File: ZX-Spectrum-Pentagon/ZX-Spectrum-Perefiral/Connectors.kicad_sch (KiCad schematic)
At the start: 4 parts, among them J1 IDE, J2 FDD

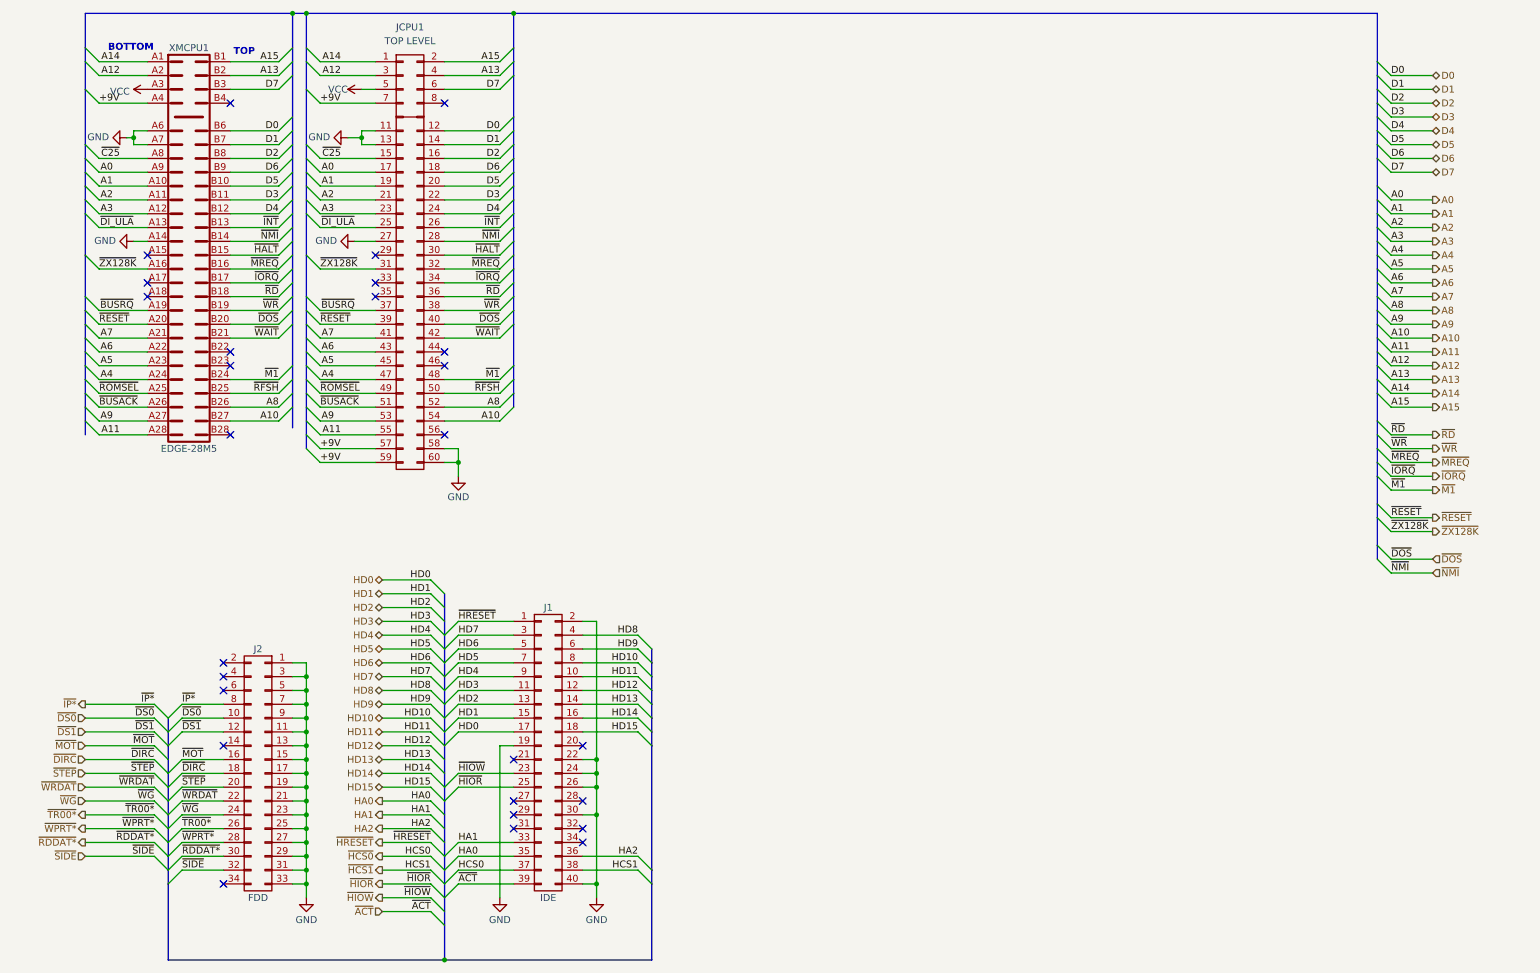
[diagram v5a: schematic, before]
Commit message: FDControlers rename from VCC1 to VDD zx_custom_symbol add connector Conn_02x32_Odd_Even ZX-Spectrum-Pentagon rename from +9V to POWER ZX-Spectrum-Perefiral improve schematic
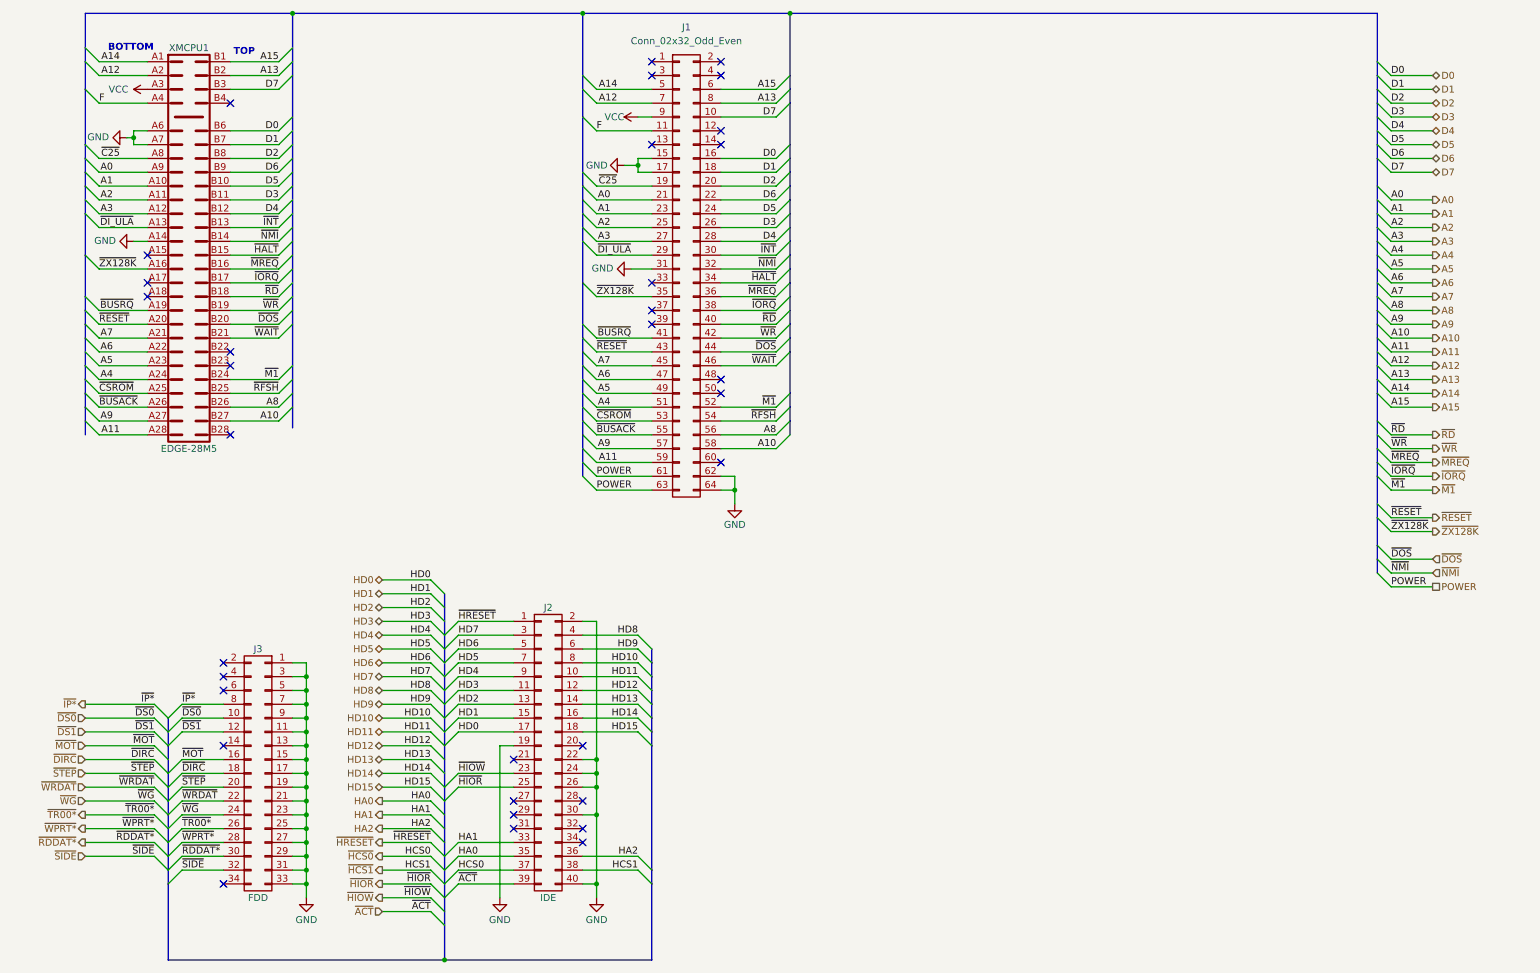
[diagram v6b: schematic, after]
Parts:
- removed JCPU1: TOP LEVEL, ZX-Spectrum-Pentagon:PinSocket_2x30_P2.54mm_Vertical, symbol zx_custom_symbol:Conn_02x30
- added J1: Conn_02x32_Odd_Even, Connector_PinSocket_2.54mm:PinSocket_2x32_P2.54mm_Vertical, symbol zx_custom_symbol:Conn_02x32_Odd_Even
- renumbered J1 to J2, J2 to J3
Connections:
- net A0: now also J1.21 (Pin_21)
- net A1: now also J1.23 (Pin_23)
- net A10: now also J1.58 (Pin_58)
- net A11: now also J1.59 (Pin_59)
- net A12: now also J1.7 (Pin_7)
- net A13: now also J1.8 (Pin_8)
- net A14: now also J1.5 (Pin_5)
- net A15: now also J1.6 (Pin_6)
- net A2: now also J1.25 (Pin_25)
- net A3: now also J1.27 (Pin_27)
- net A4: now also J1.51 (Pin_51)
- net A5: now also J1.49 (Pin_49)
- net A6: now also J1.47 (Pin_47)
- net A7: now also J1.45 (Pin_45)
- net A8: now also J1.56 (Pin_56)
- net A9: now also J1.57 (Pin_57)
- net D0: now also J1.16 (Pin_16)
- net D1: now also J1.18 (Pin_18)
- net D2: now also J1.20 (Pin_20)
- net D3: now also J1.26 (Pin_26)
- net D4: now also J1.28 (Pin_28)
- net D5: now also J1.24 (Pin_24)
- net D6: now also J1.22 (Pin_22)
- net D7: now also J1.10 (Pin_10)
- net GND: now also J1.15 (Pin_15), J1.17 (Pin_17), J1.31 (Pin_31), J1.62 (Pin_62), J1.64 (Pin_64)
- net VCC: now also J1.9 (Pin_9)
- net ~{BUSACK}: now also J1.55 (Pin_55)
- net ~{BUSRQ}: now also J1.41 (Pin_41)
- net ~{C25}: now also J1.19 (Pin_19)
- net ~{DI_ULA}: now also J1.29 (Pin_29)
- net ~{DOS}: now also J1.44 (Pin_44)
- net ~{HALT}: now also J1.34 (Pin_34)
- net ~{INT}: now also J1.30 (Pin_30)
- net ~{IORQ}: now also J1.38 (Pin_38)
- net ~{M1}: now also J1.52 (Pin_52)
- net ~{MREQ}: now also J1.36 (Pin_36)
- net ~{NMI}: now also J1.32 (Pin_32)
- net ~{RD}: now also J1.40 (Pin_40)
- net ~{RESET}: now also J1.43 (Pin_43)
- net ~{RFSH}: now also J1.54 (Pin_54)
- net ~{WAIT}: now also J1.46 (Pin_46)
- net ~{WR}: now also J1.42 (Pin_42)
- net ~{ZX128K}: now also J1.35 (Pin_35)
- net +9V renamed F
- net F: now also J1.11 (Pin_11)
- net ~{ROMSEL} renamed ~{CSROM}
- net ~{CSROM}: now also J1.53 (Pin_53)
- new net POWER: J1.61 (Pin_61), J1.63 (Pin_63)
- no-connect marks 27 -> 33
